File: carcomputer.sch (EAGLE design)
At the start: 78 parts, among them IC1 LM358N, K1 351, K2 RT184012, K3 RT184012, Q1 BS170, Q5 TIP136, T1 BC618, T2 BC618, T3 BC618, T4 BC618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

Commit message: Fixed SD module length. Refitted SPI and I2C header.
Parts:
- U$5: value HKD-MICRO-SD-BREAKOUT -> HKD-MICRO-SD-BREAKOUTH; device sd-mmc:HKD-MICRO-SD-BREAKOUT -> sd-mmc:HKD-MICRO-SD-BREAKOUTH
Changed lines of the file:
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@@
 <part name="GND21" library="supply1" library_urn="urn:adsk.eagle:library:371" deviceset="GND" device=""/>
 <part name="P+16" library="supply1" library_urn="urn:adsk.eagle:library:371" deviceset="+5V" device=""/>
-<part name="U$5" library="sd-mmc" deviceset="HKD-MICRO-SD-BREAKOUT" device=""/>
+<part name="U$5" library="sd-mmc" deviceset="HKD-MICRO-SD-BREAKOUT" device="H"/>
 <part name="GND24" library="supply1" library_urn="urn:adsk.eagle:library:371" deviceset="GND" device=""/>
 <part name="P+19" library="supply1" library_urn="urn:adsk.eagle:library:371" deviceset="+5V" device=""/>

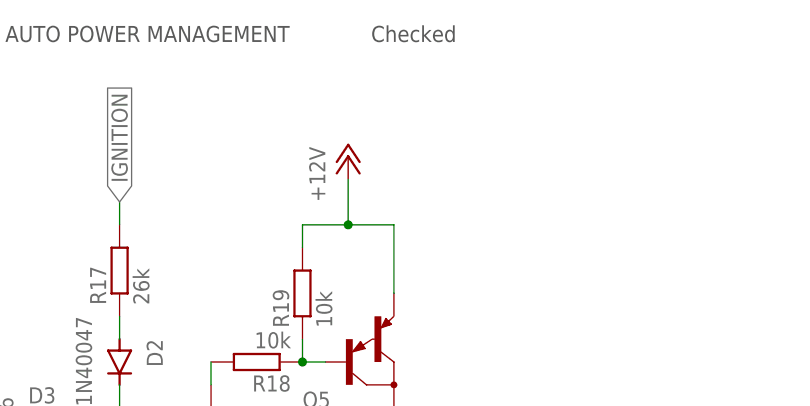
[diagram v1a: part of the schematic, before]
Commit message: Added connector for fuse. Added extra safety boundries around high voltage areas.
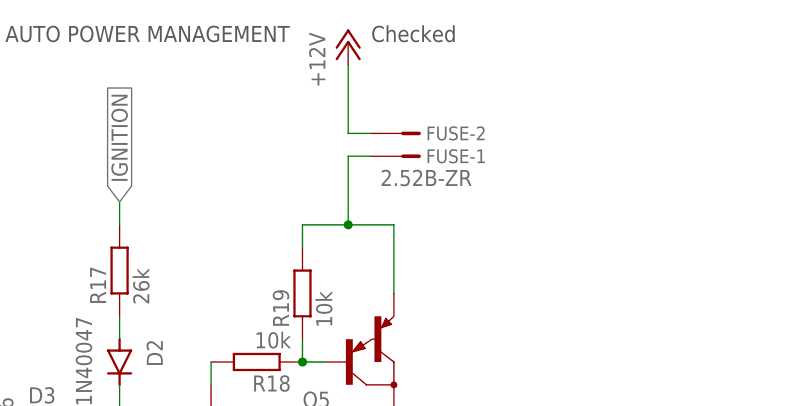
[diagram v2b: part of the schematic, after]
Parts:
- added FUSE: 2.52B-ZR, con-jst-custom:2.52B-ZR
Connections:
- new net N$21: FUSE-1.1, Q5.E, R19.2
- net +12V: now also FUSE-2.1; no longer Q5.E, R19.2
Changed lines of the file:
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@@
 <grid distance="0.1" unitdist="inch" unit="inch" style="lines" multiple="1" display="no" altdistance="0.01" altunitdist="inch" altunit="inch"/>
 <layers>
-<layer number="1" name="Top" color="4" fill="1" visible="no" active="no"/>
-<layer number="16" name="Bottom" color="1" fill="1" visible="no" active="no"/>
-<layer number="17" name="Pads" color="2" fill="1" visible="no" active="no"/>
-<layer number="18" name="Vias" color="2" fill="1" visible="no" active="no"/>
-<layer number="19" name="Unrouted" color="6" fill="1" visible="no" active="no"/>
-<layer number="20" name="Dimension" color="24" fill="1" visible="no" active="no"/>
-<layer number="21" name="tPlace" color="7" fill="1" visible="no" active="no"/>
-<layer number="22" name="bPlace" color="7" fill="1" visible="no" active="no"/>
-<layer number="23" name="tOrigins" color="15" fill="1" visible="no" active="no"/>
-<layer number="24" name="bOrigins" color="15" fill="1" visible="no" active="no"/>
-<layer number="25" name="tNames" color="7" fill="1" visible="no" active="no"/>
-<layer number="26" name="bNames" color="7" fill="1" visible="no" active="no"/>
-<layer number="27" name="tValues" color="7" fill="1" visible="no" active="no"/>
-<layer number="28" name="bValues" color="7" fill="1" visible="no" active="no"/>
+<layer number="1" name="Top" color="4" fill="1" visible="yes" active="no"/>
+<layer number="16" name="Bottom" color="1" fill="1" visible="yes" active="no"/>
+<layer number="17" name="Pads" color="2" fill="1" visible="yes" active="no"/>
+<layer number="18" name="Vias" color="2" fill="1" visible="yes" active="no"/>
+<layer number="19" name="Unrouted" color="6" fill="1" visible="yes" active="no"/>
+<layer number="20" name="Dimension" color="24" fill="1" visible="yes" active="no"/>
+<layer number="21" name="tPlace" color="7" fill="1" visible="yes" active="no"/>
+<layer number="22" name="bPlace" color="7" fill="1" visible="yes" active="no"/>
+<layer number="23" name="tOrigins" color="15" fill="1" visible="yes" active="no"/>
+<layer number="24" name="bOrigins" color="15" fill="1" visible="yes" active="no"/>
+<layer number="25" name="tNames" color="7" fill="1" visible="yes" active="no"/>
+<layer number="26" name="bNames" color="7" fill="1" visible="yes" active="no"/>
+<layer number="27" name="tValues" color="7" fill="1" visible="yes" active="no"/>
+<layer number="28" name="bValues" color="7" fill="1" visible="yes" active="no"/>
 <layer number="29" name="tStop" color="7" fill="3" visible="no" active="no"/>
 <layer number="30" name="bStop" color="7" fill="6" visible="no" active="no"/>
@@
 <layer number="35" name="tGlue" color="7" fill="4" visible="no" active="no"/>
 <layer number="36" name="bGlue" color="7" fill="5" visible="no" active="no"/>
-<layer number="37" name="tTest" color="7" fill="1" visible="no" active="no"/>
-<layer number="38" name="bTest" color="7" fill="1" visible="no" active="no"/>
+<layer number="37" name="tTest" color="7" fill="1" visible="yes" active="no"/>
+<layer number="38" name="bTest" color="7" fill="1" visible="yes" active="no"/>
 <layer number="39" name="tKeepout" color="4" fill="11" visible="no" active="no"/>
 <layer number="40" name="bKeepout" color="1" fill="11" visible="no" active="no"/>
@@
 <layer number="44" name="Drills" color="7" fill="1" visible="no" active="no"/>
 <layer number="45" name="Holes" color="7" fill="1" visible="no" active="no"/>
-<layer number="46" name="Milling" color="3" fill="1" visible="no" active="no"/>
-<layer number="47" name="Measures" color="7" fill="1" visible="no" active="no"/>
-<layer number="48" name="Document" color="7" fill="1" visible="no" active="no"/>
-<layer number="49" name="Reference" color="7" fill="1" visible="no" active="no"/>
-<layer number="50" name="dxf" color="7" fill="1" visible="no" active="no"/>
-<layer number="51" name="tDocu" color="7" fill="1" visible="no" active="no"/>
-<layer number="52" name="bDocu" color="7" fill="1" visible="no" active="no"/>
+<layer number="46" name="Milling" color="3" fill="1" visible="yes" active="no"/>
+<layer number="47" name="Measures" color="7" fill="1" visible="yes" active="no"/>
+<layer number="48" name="Document" color="7" fill="1" visible="yes" active="no"/>
+<layer number="49" name="Reference" color="7" fill="1" visible="yes" active="no"/>
+<layer number="50" name="dxf" color="7" fill="1" visible="yes" active="no"/>
+<layer number="51" name="tDocu" color="7" fill="1" visible="yes" active="no"/>
+<layer number="52" name="bDocu" color="7" fill="1" visible="yes" active="no"/>
 <layer number="88" name="SimResults" color="9" fill="1" visible="yes" active="yes"/>
 <layer number="89" name="SimProbes" color="9" fill="1" visible="yes" active="yes"/>
@@
 <part name="R24" library="rcl" library_urn="urn:adsk.eagle:library:334" deviceset="R-EU_" device="0207/7" package3d_urn="urn:adsk.eagle:package:23493/2" value="5k"/>
 <part name="R25" library="rcl" library_urn="urn:adsk.eagle:library:334" deviceset="R-EU_" device="0207/7" package3d_urn="urn:adsk.eagle:package:23493/2" value="10k"/>
+<part name="FUSE" library="con-jst-custom" deviceset="?2B-ZR" device="2.5" value="2.52B-ZR"/>
 </parts>
 <sheets>
@@
 <attribute name="VALUE" x="48.26" y="208.28" size="1.778" layer="96"/>
 </instance>
-<instance part="P+7" gate="1" x="-43.18" y="236.22" smashed="yes">
-<attribute name="VALUE" x="-45.72" y="231.14" size="1.778" layer="96" rot="R90"/>
+<instance part="P+7" gate="1" x="-43.18" y="248.92" smashed="yes">
+<attribute name="VALUE" x="-45.72" y="243.84" size="1.778" layer="96" rot="R90"/>
 </instance>
 <instance part="R6" gate="G$1" x="-68.58" y="198.12" smashed="yes" rot="R90">
@@
 <attribute name="NAME" x="234.7214" y="-24.13" size="1.778" layer="95" rot="R90"/>
 <attribute name="VALUE" x="239.522" y="-24.13" size="1.778" layer="96" rot="R90"/>
+</instance>
+<instance part="FUSE" gate="-1" x="-35.56" y="236.22" smashed="yes" rot="MR180">
+<attribute name="NAME" x="-34.544" y="236.982" size="1.524" layer="95" rot="MR180"/>
+<attribute name="VALUE" x="-39.624" y="234.696" size="1.778" layer="96" rot="MR180"/>
+</instance>
+<instance part="FUSE" gate="-2" x="-35.56" y="238.76" smashed="yes" rot="MR180">
+<attribute name="NAME" x="-34.544" y="239.522" size="1.524" layer="95" rot="MR180"/>
 </instance>
 </instances>
@@
 </segment>
 <segment>
-<wire x1="-43.18" y1="228.6" x2="-48.26" y2="228.6" width="0.1524" layer="91"/>
 <pinref part="P+7" gate="1" pin="+12V"/>
-<wire x1="-43.18" y1="233.68" x2="-43.18" y2="228.6" width="0.1524" layer="91"/>
-<pinref part="R19" gate="G$1" pin="2"/>
-<wire x1="-48.26" y1="226.06" x2="-48.26" y2="228.6" width="0.1524" layer="91"/>
-<pinref part="Q5" gate="G$1" pin="E"/>
-<wire x1="-38.1" y1="228.6" x2="-38.1" y2="220.98" width="0.1524" layer="91"/>
-<wire x1="-43.18" y1="228.6" x2="-38.1" y2="228.6" width="0.1524" layer="91"/>
-<junction x="-43.18" y="228.6"/>
+<wire x1="-43.18" y1="246.38" x2="-43.18" y2="238.76" width="0.1524" layer="91"/>
+<pinref part="FUSE" gate="-2" pin="1"/>
+<wire x1="-43.18" y1="238.76" x2="-40.64" y2="238.76" width="0.1524" layer="91"/>
 </segment>
 </net>
@@
 </segment>
 </net>
+<net name="N$21" class="0">
+<segment>
+<pinref part="R19" gate="G$1" pin="2"/>
+<wire x1="-48.26" y1="226.06" x2="-48.26" y2="228.6" width="0.1524" layer="91"/>
+<pinref part="Q5" gate="G$1" pin="E"/>
+<wire x1="-38.1" y1="228.6" x2="-38.1" y2="220.98" width="0.1524" layer="91"/>
+<wire x1="-48.26" y1="228.6" x2="-43.18" y2="228.6" width="0.1524" layer="91"/>
+<wire x1="-43.18" y1="228.6" x2="-38.1" y2="228.6" width="0.1524" layer="91"/>
+<wire x1="-43.18" y1="236.22" x2="-43.18" y2="228.6" width="0.1524" layer="91"/>
+<junction x="-43.18" y="228.6"/>
+<pinref part="FUSE" gate="-1" pin="1"/>
+<wire x1="-40.64" y1="236.22" x2="-43.18" y2="236.22" width="0.1524" layer="91"/>
+</segment>
+</net>

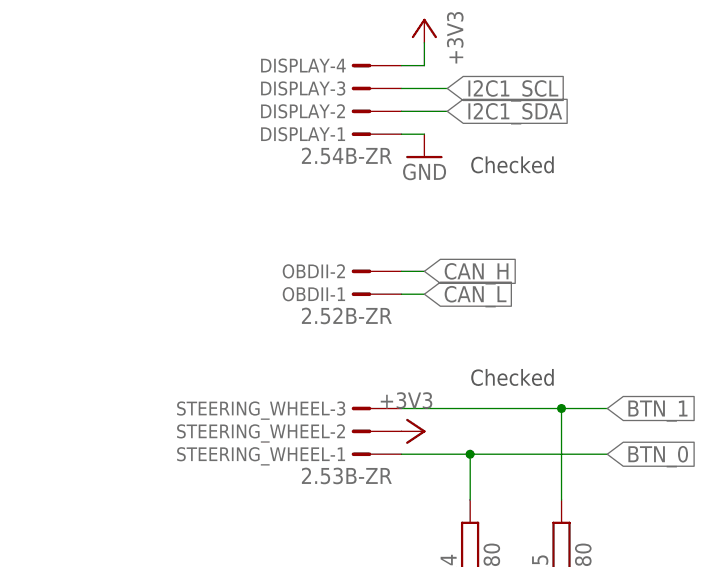
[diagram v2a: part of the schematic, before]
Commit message: Renamed OBDII to CAN
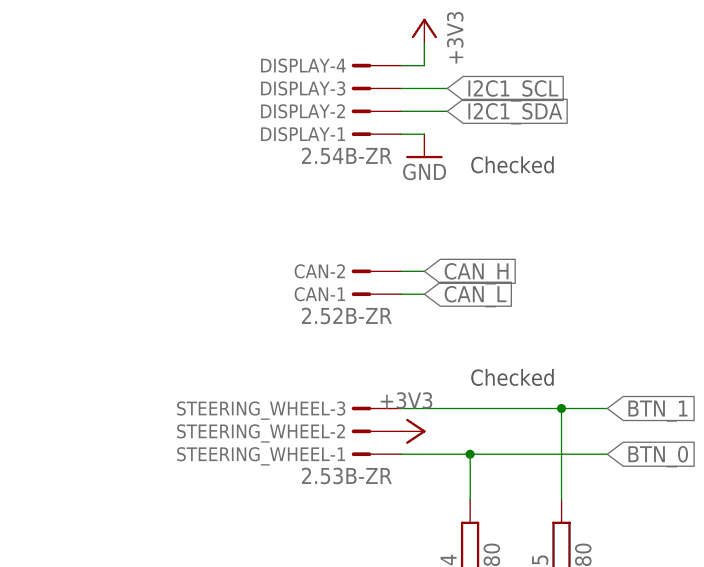
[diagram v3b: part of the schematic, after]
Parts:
- renumbered OBDII to CAN
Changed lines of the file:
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@@
 <grid distance="0.1" unitdist="inch" unit="inch" style="lines" multiple="1" display="no" altdistance="0.01" altunitdist="inch" altunit="inch"/>
 <layers>
-<layer number="1" name="Top" color="4" fill="1" visible="yes" active="no"/>
-<layer number="16" name="Bottom" color="1" fill="1" visible="yes" active="no"/>
-<layer number="17" name="Pads" color="2" fill="1" visible="yes" active="no"/>
-<layer number="18" name="Vias" color="2" fill="1" visible="yes" active="no"/>
-<layer number="19" name="Unrouted" color="6" fill="1" visible="yes" active="no"/>
-<layer number="20" name="Dimension" color="24" fill="1" visible="yes" active="no"/>
-<layer number="21" name="tPlace" color="7" fill="1" visible="yes" active="no"/>
-<layer number="22" name="bPlace" color="7" fill="1" visible="yes" active="no"/>
-<layer number="23" name="tOrigins" color="15" fill="1" visible="yes" active="no"/>
-<layer number="24" name="bOrigins" color="15" fill="1" visible="yes" active="no"/>
-<layer number="25" name="tNames" color="7" fill="1" visible="yes" active="no"/>
-<layer number="26" name="bNames" color="7" fill="1" visible="yes" active="no"/>
-<layer number="27" name="tValues" color="7" fill="1" visible="yes" active="no"/>
-<layer number="28" name="bValues" color="7" fill="1" visible="yes" active="no"/>
+<layer number="1" name="Top" color="4" fill="1" visible="no" active="no"/>
+<layer number="16" name="Bottom" color="1" fill="1" visible="no" active="no"/>
+<layer number="17" name="Pads" color="2" fill="1" visible="no" active="no"/>
+<layer number="18" name="Vias" color="2" fill="1" visible="no" active="no"/>
+<layer number="19" name="Unrouted" color="6" fill="1" visible="no" active="no"/>
+<layer number="20" name="Dimension" color="24" fill="1" visible="no" active="no"/>
+<layer number="21" name="tPlace" color="7" fill="1" visible="no" active="no"/>
+<layer number="22" name="bPlace" color="7" fill="1" visible="no" active="no"/>
+<layer number="23" name="tOrigins" color="15" fill="1" visible="no" active="no"/>
+<layer number="24" name="bOrigins" color="15" fill="1" visible="no" active="no"/>
+<layer number="25" name="tNames" color="7" fill="1" visible="no" active="no"/>
+<layer number="26" name="bNames" color="7" fill="1" visible="no" active="no"/>
+<layer number="27" name="tValues" color="7" fill="1" visible="no" active="no"/>
+<layer number="28" name="bValues" color="7" fill="1" visible="no" active="no"/>
 <layer number="29" name="tStop" color="7" fill="3" visible="no" active="no"/>
 <layer number="30" name="bStop" color="7" fill="6" visible="no" active="no"/>
@@
 <layer number="35" name="tGlue" color="7" fill="4" visible="no" active="no"/>
 <layer number="36" name="bGlue" color="7" fill="5" visible="no" active="no"/>
-<layer number="37" name="tTest" color="7" fill="1" visible="yes" active="no"/>
-<layer number="38" name="bTest" color="7" fill="1" visible="yes" active="no"/>
+<layer number="37" name="tTest" color="7" fill="1" visible="no" active="no"/>
+<layer number="38" name="bTest" color="7" fill="1" visible="no" active="no"/>
 <layer number="39" name="tKeepout" color="4" fill="11" visible="no" active="no"/>
 <layer number="40" name="bKeepout" color="1" fill="11" visible="no" active="no"/>
@@
 <layer number="44" name="Drills" color="7" fill="1" visible="no" active="no"/>
 <layer number="45" name="Holes" color="7" fill="1" visible="no" active="no"/>
-<layer number="46" name="Milling" color="3" fill="1" visible="yes" active="no"/>
-<layer number="47" name="Measures" color="7" fill="1" visible="yes" active="no"/>
-<layer number="48" name="Document" color="7" fill="1" visible="yes" active="no"/>
-<layer number="49" name="Reference" color="7" fill="1" visible="yes" active="no"/>
-<layer number="50" name="dxf" color="7" fill="1" visible="yes" active="no"/>
-<layer number="51" name="tDocu" color="7" fill="1" visible="yes" active="no"/>
-<layer number="52" name="bDocu" color="7" fill="1" visible="yes" active="no"/>
+<layer number="46" name="Milling" color="3" fill="1" visible="no" active="no"/>
+<layer number="47" name="Measures" color="7" fill="1" visible="no" active="no"/>
+<layer number="48" name="Document" color="7" fill="1" visible="no" active="no"/>
+<layer number="49" name="Reference" color="7" fill="1" visible="no" active="no"/>
+<layer number="50" name="dxf" color="7" fill="1" visible="no" active="no"/>
+<layer number="51" name="tDocu" color="7" fill="1" visible="no" active="no"/>
+<layer number="52" name="bDocu" color="7" fill="1" visible="no" active="no"/>
 <layer number="88" name="SimResults" color="9" fill="1" visible="yes" active="yes"/>
 <layer number="89" name="SimProbes" color="9" fill="1" visible="yes" active="yes"/>
@@
 <part name="GND8" library="supply1" library_urn="urn:adsk.eagle:library:371" deviceset="GND" device=""/>
 <part name="GND9" library="supply1" library_urn="urn:adsk.eagle:library:371" deviceset="GND" device=""/>
-<part name="OBDII" library="con-jst-custom" deviceset="?2B-ZR" device="2.5" value="2.52B-ZR"/>
+<part name="CAN" library="con-jst-custom" deviceset="?2B-ZR" device="2.5" value="2.52B-ZR"/>
 <part name="U$4" library="PSU" deviceset="LM2596S" device=""/>
 <part name="GND11" library="supply1" library_urn="urn:adsk.eagle:library:371" deviceset="GND" device=""/>
@@
 <attribute name="VALUE" x="-30.48" y="83.82" size="1.778" layer="96"/>
 </instance>
-<instance part="OBDII" gate="-1" x="-167.64" y="96.52" smashed="yes" rot="R180">
+<instance part="CAN" gate="-1" x="-167.64" y="96.52" smashed="yes" rot="R180">
 <attribute name="NAME" x="-168.656" y="97.282" size="1.524" layer="95" rot="R180"/>
 <attribute name="VALUE" x="-163.576" y="94.996" size="1.778" layer="96" rot="R180"/>
 </instance>
-<instance part="OBDII" gate="-2" x="-167.64" y="99.06" smashed="yes" rot="R180">
+<instance part="CAN" gate="-2" x="-167.64" y="99.06" smashed="yes" rot="R180">
 <attribute name="NAME" x="-168.656" y="99.822" size="1.524" layer="95" rot="R180"/>
 </instance>
@@
 </segment>
 <segment>
-<pinref part="OBDII" gate="-2" pin="1"/>
+<pinref part="CAN" gate="-2" pin="1"/>
 <wire x1="-162.56" y1="99.06" x2="-160.02" y2="99.06" width="0.1524" layer="91"/>
 <label x="-160.02" y="99.06" size="1.778" layer="95" xref="yes"/>
@@
 </segment>
 <segment>
-<pinref part="OBDII" gate="-1" pin="1"/>
+<pinref part="CAN" gate="-1" pin="1"/>
 <wire x1="-162.56" y1="96.52" x2="-160.02" y2="96.52" width="0.1524" layer="91"/>
 <label x="-160.02" y="96.52" size="1.778" layer="95" xref="yes"/>
